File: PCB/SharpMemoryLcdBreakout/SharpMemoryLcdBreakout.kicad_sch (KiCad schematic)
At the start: 10 parts, among them J1 EMD, J2 DISP, J3 EIN, J4 Conn_2Rows-05Pins, J5 FH12-10S-0.5SH

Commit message: increased size of pcb for smt assembly
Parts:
- C1, C2, C3: LCSC (none) -> C14663
- J5: LCSC (none) -> C506791
- R1, R2: LCSC (none) -> C25804
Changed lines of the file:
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@@
+      (effects (font (size 1.27 1.27)) hide)
+    )
+    (property "LCSC" "C25804" (id 4) (at 114.046 33.782 90)
       (effects (font (size 1.27 1.27)) hide)
     )
@@
     )
     (property "Datasheet" "~" (id 3) (at 122.682 33.782 0)
+      (effects (font (size 1.27 1.27)) hide)
+    )
+    (property "LCSC" "C25804" (id 4) (at 122.682 33.782 90)
       (effects (font (size 1.27 1.27)) hide)
     )
@@
       (effects (font (size 1.27 1.27)) hide)
     )
+    (property "LCSC" "C14663" (id 4) (at 134.874 68.834 0)
+      (effects (font (size 1.27 1.27)) hide)
+    )
     (pin "1")
     (pin "2")
@@
       (effects (font (size 1.27 1.27)) hide)
     )
+    (property "LCSC" "C14663" (id 4) (at 146.304 68.834 0)
+      (effects (font (size 1.27 1.27)) hide)
+    )
     (pin "1")
     (pin "2")
@@
     )
     (property "Datasheet" "~" (id 3) (at 157.988 68.834 0)
+      (effects (font (size 1.27 1.27)) hide)
+    )
+    (property "LCSC" "C14663" (id 4) (at 157.988 68.834 0)
       (effects (font (size 1.27 1.27)) hide)
     )
@@
       (effects (font (size 1.27 1.27)) hide)
     )
+    (property "LCSC" "C506791" (id 4) (at 170.18 44.196 0)
+      (effects (font (size 1.27 1.27)) hide)
+    )

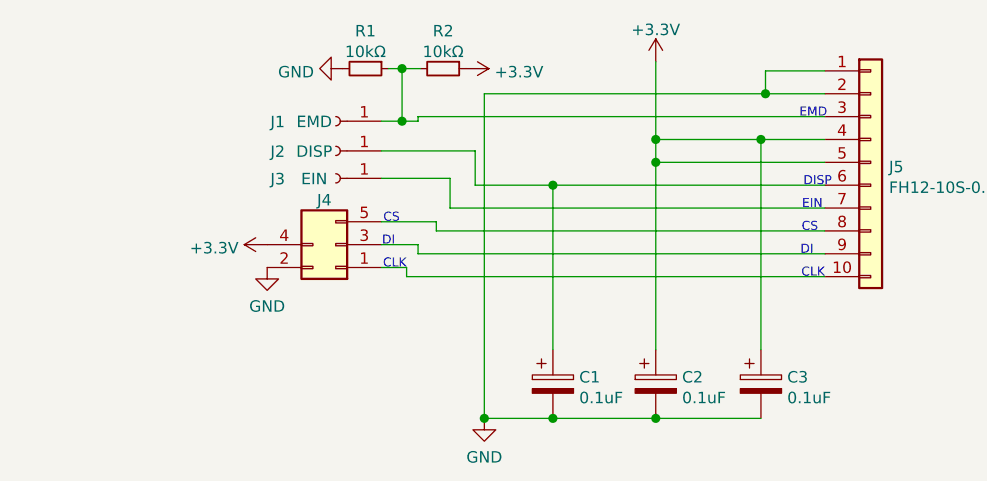
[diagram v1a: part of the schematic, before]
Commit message: added pins for disp and emd
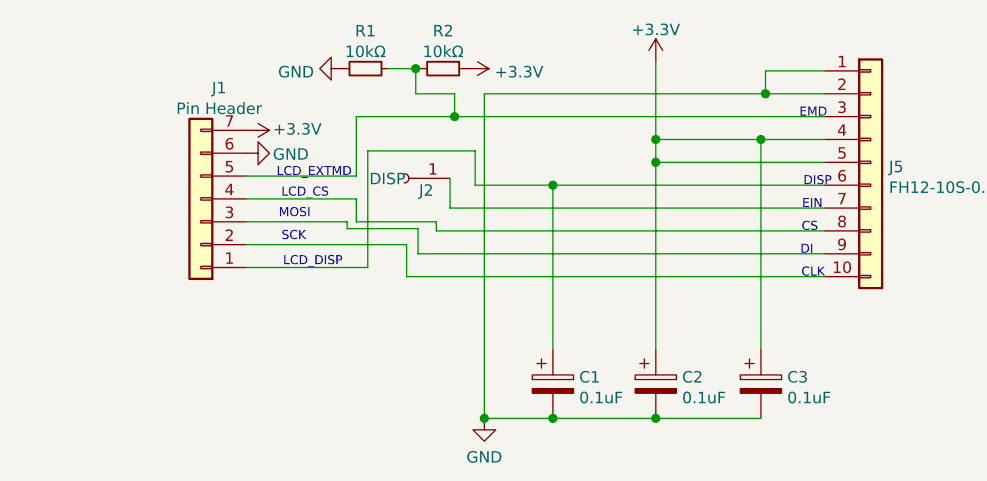
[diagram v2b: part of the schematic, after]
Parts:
- removed J1: EMD, TestPoint:TestPoint_Pad_D1.5mm, symbol Connector:Conn_01x01_Female
- removed J3: EIN, TestPoint:TestPoint_Pad_D1.5mm, symbol Connector:Conn_01x01_Female
- removed J4: Conn_2Rows-05Pins, SharpMemoryLcdBreakout:PinHeader_2Rows-05Pins_P2.54mm_Vertical, symbol Connector_Generic:Conn_2Rows-05Pins
- added J1: Pin Header, SharpMemoryLcdBreakout:PinSocket_2Row_5+3_P2.54mm_Vertical, symbol Connector_Generic:Conn_01x07
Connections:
- net +3V3: now also J1.7 (Pin_7)
- net GND: now also J1.6 (Pin_6)
- net at J5.10 (Pin_10): now also J1.2 (Pin_2)
- net at J5.9 (Pin_9): now also J1.3 (Pin_3)
- net at J5.8 (Pin_8): now also J1.4 (Pin_4)
- net at J5.3 (Pin_3), R1.1, R2.2: now also J1.5 (Pin_5)
- net at C1.1, J5.6 (Pin_6): now also J1.1 (Pin_1); no longer J2.1 (Pin_1)
- net at J5.7 (Pin_7): now also J2.1 (Pin_1)
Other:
- note added: "LCD_CS"
- note added: "LCD_DISP"
- note added: "LCD_EXTMD"
- note added: "MOSI"
- note added: "SCK"

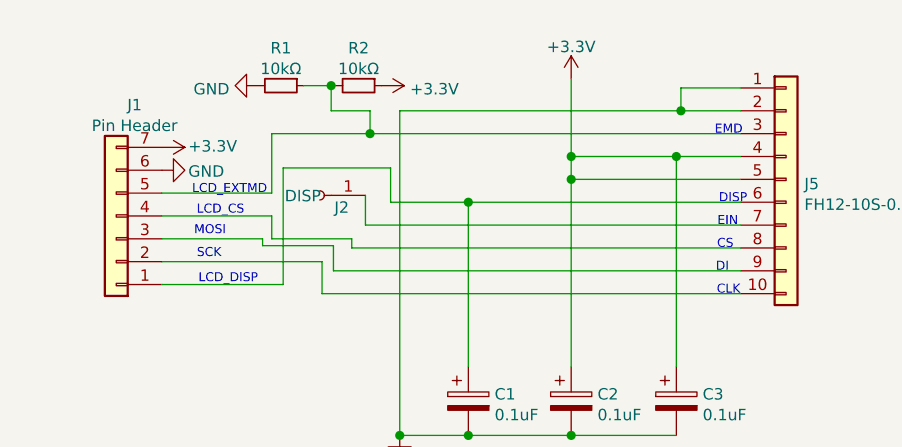
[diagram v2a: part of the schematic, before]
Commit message: switched EIN and EMD pin connections
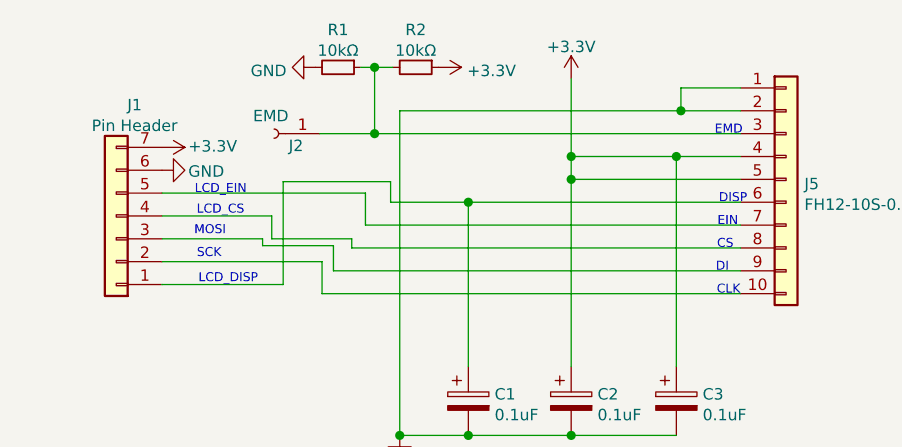
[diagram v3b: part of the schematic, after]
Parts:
- J2: value DISP -> EMD
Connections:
- net at J5.3 (Pin_3), R1.1, R2.2: now also J2.1 (Pin_1); no longer J1.5 (Pin_5)
- net at J5.7 (Pin_7): now also J1.5 (Pin_5); no longer J2.1 (Pin_1)
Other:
- note added: "LCD_EIN"
- note removed: "LCD_EXTMD"
- moved on the sheet: J2, R1, R2

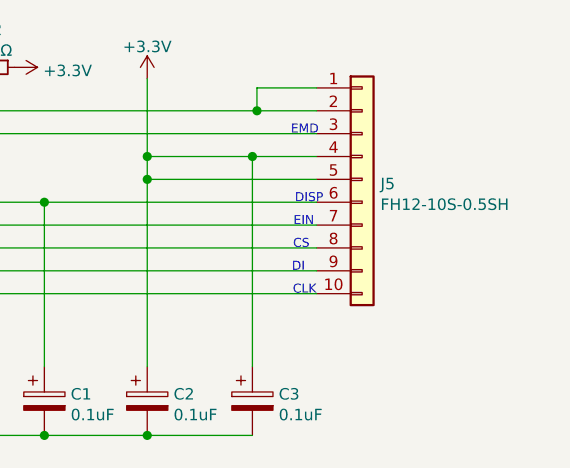
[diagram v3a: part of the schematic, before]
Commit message: Mirrored FPC pins
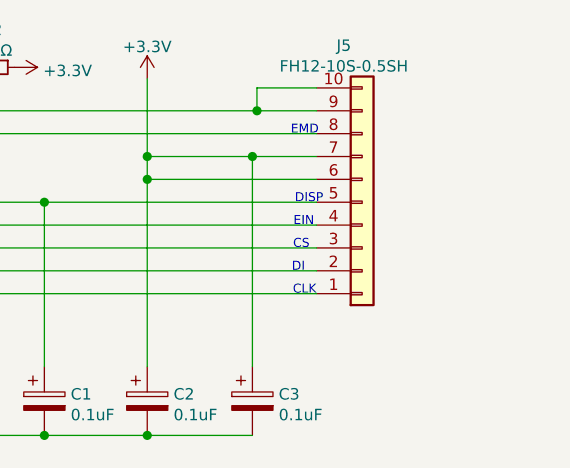
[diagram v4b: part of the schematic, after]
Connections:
- net +3V3: now also J5.6 (Pin_6), J5.7 (Pin_7); no longer J5.4 (Pin_4), J5.5 (Pin_5)
- net GND: now also J5.10 (Pin_10), J5.9 (Pin_9); no longer J5.1 (Pin_1), J5.2 (Pin_2)
- net at C1.1, J1.1 (Pin_1): now also J5.5 (Pin_5); no longer J5.6 (Pin_6)
- net at J1.2 (Pin_2): now also J5.1 (Pin_1); no longer J5.10 (Pin_10)
- net at J1.3 (Pin_3): now also J5.2 (Pin_2); no longer J5.9 (Pin_9)
- net at J1.4 (Pin_4): now also J5.3 (Pin_3); no longer J5.8 (Pin_8)
- net at J1.5 (Pin_5): now also J5.4 (Pin_4); no longer J5.7 (Pin_7)
- net at J2.1 (Pin_1), R1.1, R2.2: now also J5.8 (Pin_8); no longer J5.3 (Pin_3)
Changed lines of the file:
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@@
     (pin "7")
   )
-  (symbol (lib_id "Connector_Generic:Conn_01x10") (at 170.18 44.196 0) (unit 1)
+  (symbol (lib_id "Connector_Generic:Conn_01x10") (at 170.18 46.736 0) (mirror x) (unit 1)
     (in_bom yes) (on_board yes) (fields_autoplaced)
-    (property "Reference" "J5" (id 0) (at 172.2121 44.7051 0)
-      (effects (font (size 1.27 1.27)) (justify left))
-    )
-    (property "Value" "FH12-10S-0.5SH" (id 1) (at 172.2121 47.0038 0)
-      (effects (font (size 1.27 1.27)) (justify left))
-    )
-    (property "Footprint" "Connector_FFC-FPC:Hirose_FH12-10S-0.5SH_1x10-1MP_P0.50mm_Horizontal" (id 2) (at 170.18 44.196 0)
+    (property "Reference" "J5" (id 0) (at 168.148 29.3328 0))
+    (property "Value" "FH12-10S-0.5SH" (id 1) (at 168.148 31.6315 0))
+    (property "Footprint" "Connector_FFC-FPC:Hirose_FH12-10S-0.5SH_1x10-1MP_P0.50mm_Horizontal" (id 2) (at 170.18 46.736 0)
       (effects (font (size 1.27 1.27)) hide)
     )
-    (property "Datasheet" "~" (id 3) (at 170.18 44.196 0)
+    (property "Datasheet" "~" (id 3) (at 170.18 46.736 0)
       (effects (font (size 1.27 1.27)) hide)
     )
-    (property "LCSC" "C506791" (id 4) (at 170.18 44.196 0)
+    (property "LCSC" "C506791" (id 4) (at 170.18 46.736 0)
       (effects (font (size 1.27 1.27)) hide)
     )

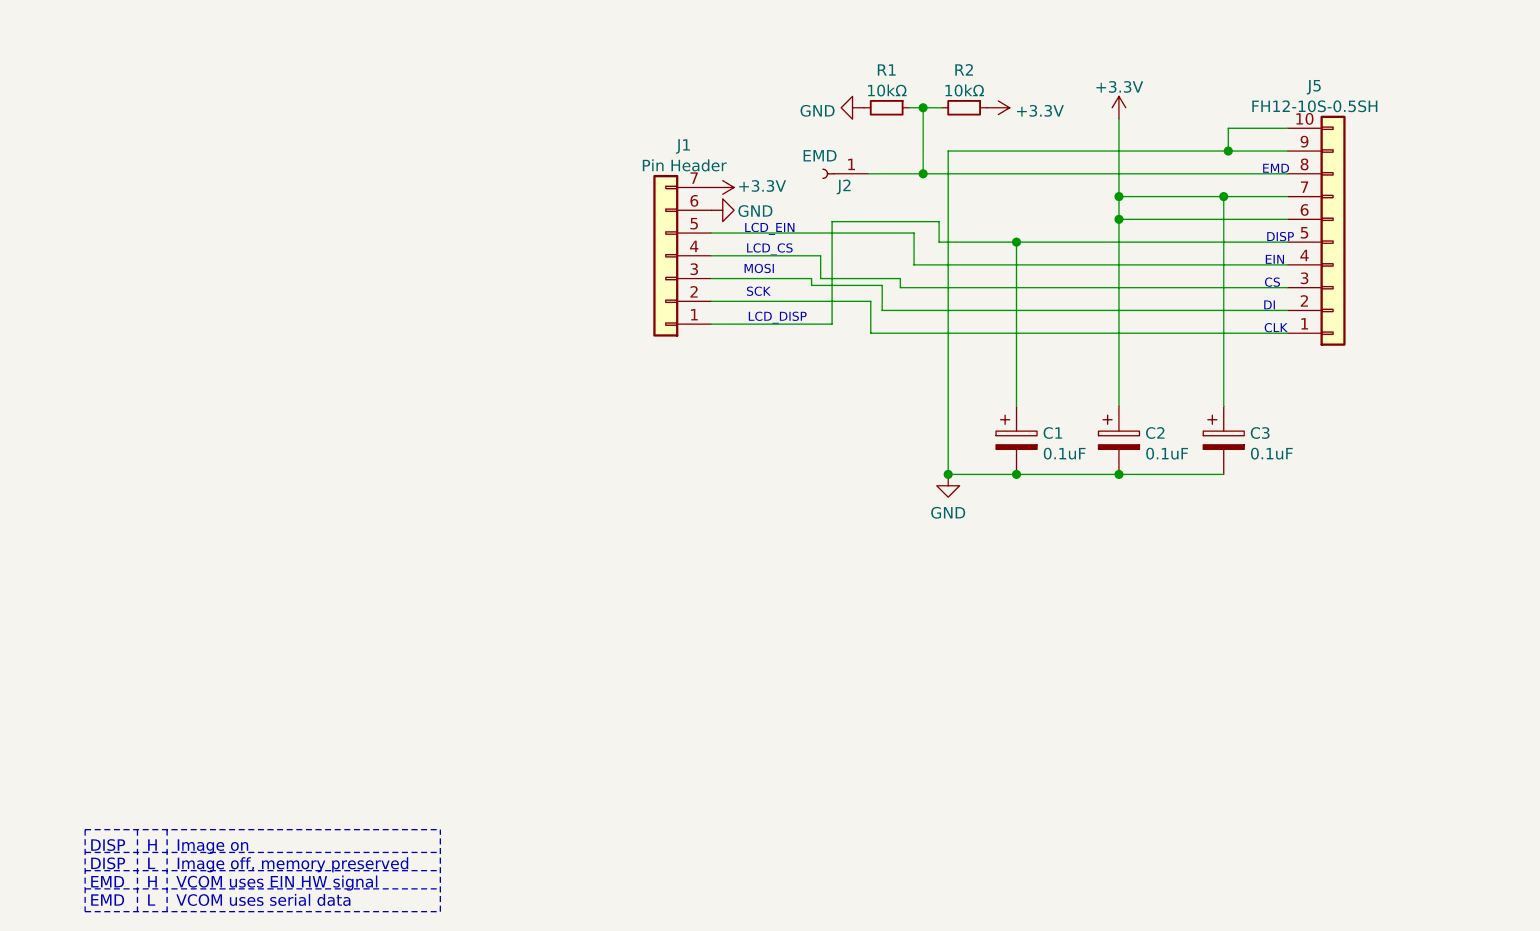
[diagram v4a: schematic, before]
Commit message: increased part size (0805) and improved silk screen and added ferrite beads
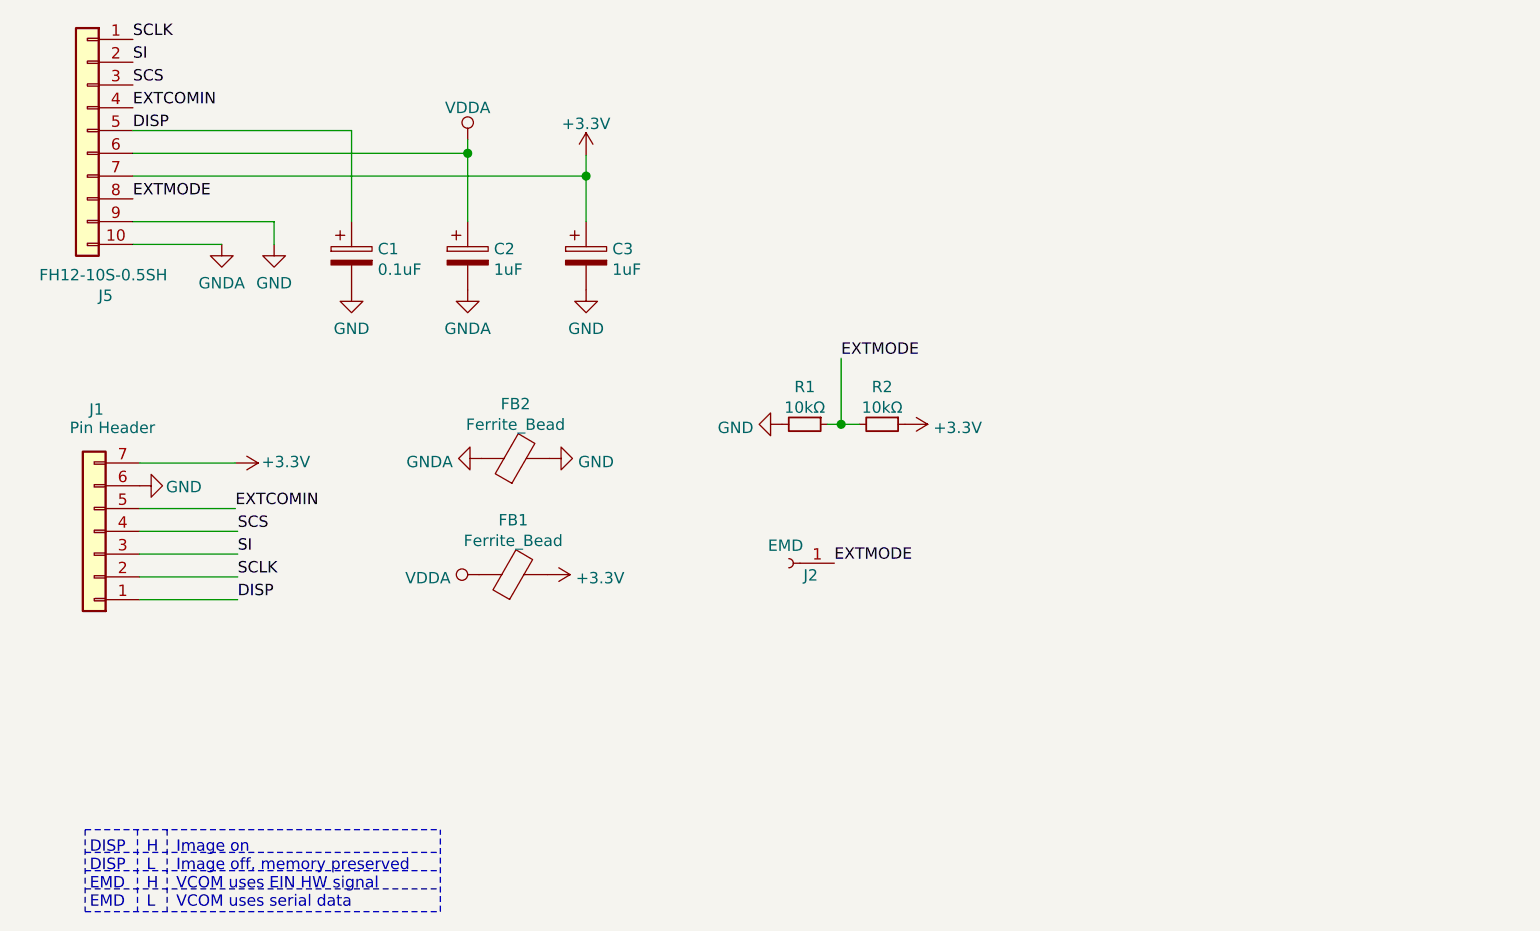
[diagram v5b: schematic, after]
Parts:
- added FB1, FB2: Ferrite_Bead, Resistor_SMD:R_0805_2012Metric_Pad1.15x1.40mm_HandSolder, symbol Device:Ferrite_Bead
- C1: footprint Capacitor_SMD:C_0603_1608Metric_Pad1.05x0.95mm_HandSolder -> Capacitor_SMD:C_0805_2012Metric_Pad1.15x1.40mm_HandSolder
- C2, C3: value 0.1uF -> 1uF; footprint Capacitor_SMD:C_0603_1608Metric_Pad1.05x0.95mm_HandSolder -> Capacitor_SMD:C_0805_2012Metric_Pad1.15x1.40mm_HandSolder
- R1, R2: footprint Resistor_SMD:R_0603_1608Metric_Pad1.05x0.95mm_HandSolder -> Resistor_SMD:R_0805_2012Metric_Pad1.15x1.40mm_HandSolder
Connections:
- net +3V3: now also FB1.2; no longer C2.1, J5.6 (Pin_6)
- net GND: now also FB2.2; no longer C2.2, J5.10 (Pin_10)
- net DISP: now reaches C1.1, J1.1 (Pin_1), J5.5 (Pin_5)
- net SCLK: now reaches J1.2 (Pin_2), J5.1 (Pin_1)
- net SI: now reaches J1.3 (Pin_3), J5.2 (Pin_2)
- net SCS: now reaches J1.4 (Pin_4), J5.3 (Pin_3)
- net EXTCOMIN: now reaches J1.5 (Pin_5), J5.4 (Pin_4)
- net EXTMODE: now reaches J2.1 (Pin_1), J5.8 (Pin_8), R1.1, R2.2
- new net GNDA: C2.2, FB2.1, J5.10 (Pin_10)
- new net VDDA: C2.1, FB1.1, J5.6 (Pin_6)
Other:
- note removed: "CLK"
- note removed: "CS"
- note removed: "DI"
- note removed: "DISP"
- note removed: "EIN"
- note removed: "EMD"
- note removed: "LCD_CS"
- note removed: "LCD_DISP"
- note removed: "LCD_EIN"
- note removed: "MOSI"
- note removed: "SCK"
- moved on the sheet: C1, C2, C3, J1, J2, J5, R1, R2

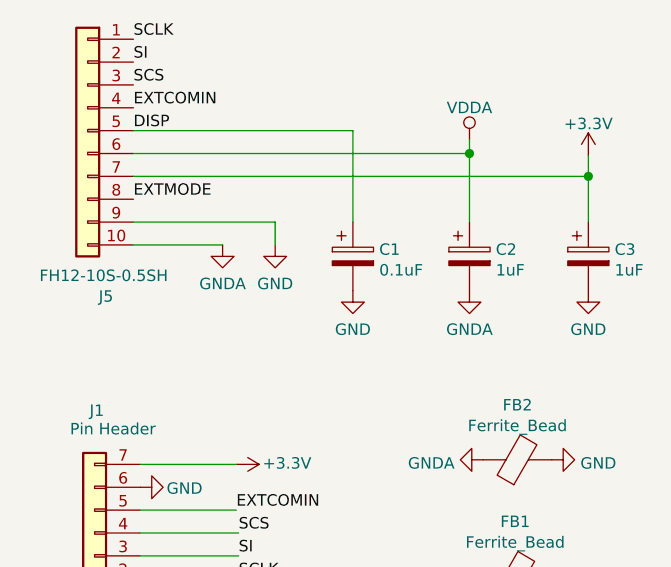
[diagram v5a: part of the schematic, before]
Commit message: Added BOM to readme and updated LCSC parts
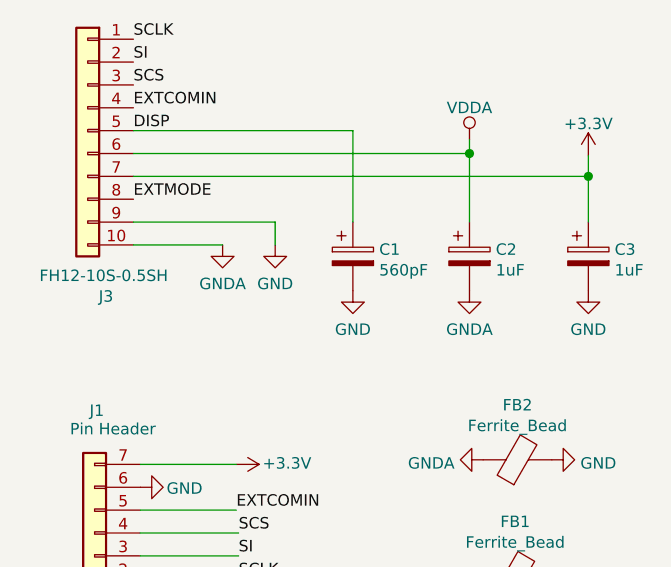
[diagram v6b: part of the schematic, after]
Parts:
- C1: value 0.1uF -> 560pF; LCSC C14663 -> C107119
- C2, C3: LCSC C14663 -> C28323
- R1, R2: LCSC C25804 -> C365230
- renumbered J5 to J3
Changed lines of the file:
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@@
       (effects (font (size 1.27 1.27)) hide)
     )
-    (property "LCSC" "C25804" (id 4) (at 111.252 67.056 90)
+    (property "LCSC" "C365230" (id 4) (at 111.252 67.056 90)
       (effects (font (size 1.27 1.27)) hide)
     )
@@
       (effects (font (size 1.27 1.27)) hide)
     )
-    (property "LCSC" "C25804" (id 4) (at 119.888 67.056 90)
+    (property "LCSC" "C365230" (id 4) (at 119.888 67.056 90)
       (effects (font (size 1.27 1.27)) hide)
     )
@@
       (effects (font (size 1.27 1.27)) (justify left))
     )
-    (property "Value" "0.1uF" (id 1) (at 63.6271 49.7978 0)
+    (property "Value" "560pF" (id 1) (at 63.6271 49.7978 0)
       (effects (font (size 1.27 1.27)) (justify left))
     )
@@
       (effects (font (size 1.27 1.27)) hide)
     )
-    (property "LCSC" "C14663" (id 4) (at 60.706 48.26 0)
+    (property "LCSC" "C107119" (id 4) (at 60.706 48.26 0)
       (effects (font (size 1.27 1.27)) hide)
     )
@@
       (effects (font (size 1.27 1.27)) hide)
     )
-    (property "LCSC" "C14663" (id 4) (at 73.66 48.26 0)
+    (property "LCSC" "C28323" (id 4) (at 73.66 48.26 0)
       (effects (font (size 1.27 1.27)) hide)
     )
@@
       (effects (font (size 1.27 1.27)) hide)
     )
-    (property "LCSC" "C14663" (id 4) (at 86.868 48.26 0)
+    (property "LCSC" "C28323" (id 4) (at 86.868 48.26 0)
       (effects (font (size 1.27 1.27)) hide)
     )
@@
   (symbol (lib_id "Connector_Generic:Conn_01x10") (at 31.242 34.29 0) (mirror y) (unit 1)
     (in_bom yes) (on_board yes)
-    (property "Reference" "J5" (id 0) (at 33.274 52.7092 0))
+    (property "Reference" "J3" (id 0) (at 33.274 52.7092 0))
     (property "Value" "FH12-10S-0.5SH" (id 1) (at 33.02 50.4105 0))
     (property "Footprint" "Connector_FFC-FPC:Hirose_FH12-10S-0.5SH_1x10-1MP_P0.50mm_Horizontal" (id 2) (at 31.242 34.29 0)
@@
     )
     (path "/7a602df9-b4ab-4c8f-bcee-115ea78044b1"
-      (reference "C1") (unit 1) (value "0.1uF") (footprint "Capacitor_SMD:C_0805_2012Metric_Pad1.15x1.40mm_HandSolder")
+      (reference "C1") (unit 1) (value "560pF") (footprint "Capacitor_SMD:C_0805_2012Metric_Pad1.15x1.40mm_HandSolder")
     )
     (path "/83e00d4f-b880-41eb-a80c-47548e30c913"
@@
     )
     (path "/865617f0-df77-422e-ba2a-73c970ba048e"
-      (reference "J5") (unit 1) (value "FH12-10S-0.5SH") (footprint "Connector_FFC-FPC:Hirose_FH12-10S-0.5SH_1x10-1MP_P0.50mm_Horizontal")
+      (reference "J3") (unit 1) (value "FH12-10S-0.5SH") (footprint "Connector_FFC-FPC:Hirose_FH12-10S-0.5SH_1x10-1MP_P0.50mm_Horizontal")
     )
     (path "/26fa69b4-96a4-485c-8f3c-4f68027d84ab"
